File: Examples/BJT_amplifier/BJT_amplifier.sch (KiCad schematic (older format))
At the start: 12 parts, among them Q1 NPN

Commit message: Modified Example
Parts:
- R1, R2, R3, R4, R5, R6: symbol R -> R-RESCUE-BJT_amplifier
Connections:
- net labels added: out
- wire segments 24 -> 26
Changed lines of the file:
@@
 EESchema Schematic File Version 2
+LIBS:BJT_amplifier-rescue
+LIBS:eSim_Analog
+LIBS:eSim_Devices
+LIBS:eSim_Digital
+LIBS:eSim_Hybrid
+LIBS:eSim_Miscellaneous
+LIBS:eSim_Sources
+LIBS:eSim_Subckt
+LIBS:eSim_User
 LIBS:power
 LIBS:device
@@
 LIBS:memory
 LIBS:xilinx
-LIBS:special
 LIBS:microcontrollers
 LIBS:dsp
@@
 LIBS:contrib
 LIBS:valves
-LIBS:eSim_Analog
-LIBS:eSim_Devices
-LIBS:eSim_Digital
-LIBS:eSim_Hybrid
-LIBS:eSim_Sources
 LIBS:BJT_amplifier-cache
 EELAYER 25 0
@@
 $EndComp
 $Comp
-L GND #PWR02
+L GND-RESCUE-BJT_amplifier #PWR02
 U 1 1 51A47FCD
 P 5650 4850
@@
 $EndComp
 $Comp
-L R R1
+L R-RESCUE-BJT_amplifier R1
 U 1 1 51A47FBC
 P 4050 3600
@@
 $EndComp
 $Comp
-L R R2
+L R-RESCUE-BJT_amplifier R2
 U 1 1 51A47FAB
 P 5100 3050
@@
 $EndComp
 $Comp
-L R R3
+L R-RESCUE-BJT_amplifier R3
 U 1 1 51A47F97
 P 5100 4200
@@
 $EndComp
 $Comp
-L R R6
+L R-RESCUE-BJT_amplifier R6
 U 1 1 51A47F8B
 P 7050 4200
@@
 $EndComp
 $Comp
-L R R5
+L R-RESCUE-BJT_amplifier R5
 U 1 1 51A47F5C
 P 6100 3050
@@
 $EndComp
 $Comp
-L R R4
+L R-RESCUE-BJT_amplifier R4
 U 1 1 51A47F50
 P 5850 4200
@@
 Wire Wire Line
 	5100 2900 5100 2800
+Text GLabel 7000 3250 2    60   Input ~ 0
+out
+Wire Wire Line
+	7000 3250 6950 3250
+Wire Wire Line
+	6950 3250 6950 3300
+Connection ~ 6950 3300
 $EndSCHEMATC

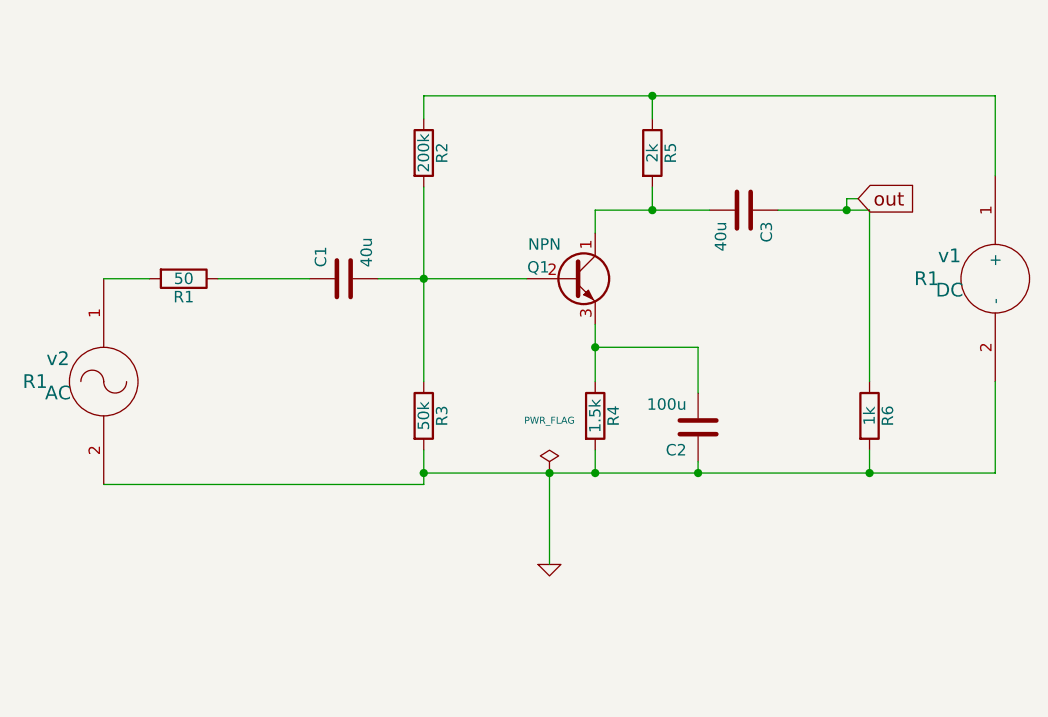
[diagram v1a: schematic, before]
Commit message: Remove unwanted example
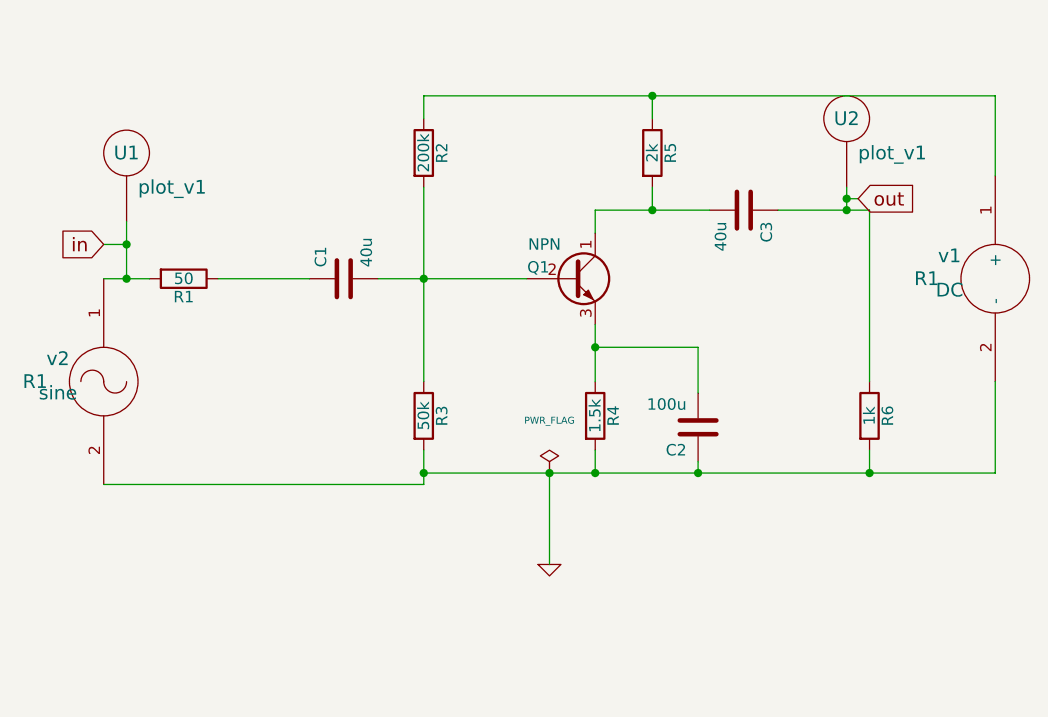
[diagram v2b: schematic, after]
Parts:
- removed v2: AC, R1, symbol AC
- added U1, U2: plot_v1, symbol plot_v1
- added v2: sine, R1, symbol sine
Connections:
- net GND: now also v2.2 (-)
- net out: now also U2.~
- net in: now reaches R1.2
- net in: now also U1.~, v2.1 (+)
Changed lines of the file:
@@
 LIBS:eSim_Hybrid
 LIBS:eSim_Miscellaneous
+LIBS:eSim_Plot
+LIBS:eSim_Power
 LIBS:eSim_Sources
 LIBS:eSim_Subckt
@@
 $EndComp
 $Comp
-L AC v2
-U 1 1 51A486A5
-P 3700 4050
-F 0 "v2" H 3500 4150 60  0000 C CNN
-F 1 "AC" H 3500 4000 60  0000 C CNN
-F 2 "R1" H 3400 4050 60  0000 C CNN
-F 3 "" H 3700 4050 60  0001 C CNN
-	1    3700 4050
-	1    0    0    -1
-$EndComp
-$Comp
 L PWR_FLAG #FLG01
 U 1 1 51A48298
@@
 	7000 3250 6950 3250
 Wire Wire Line
-	6950 3250 6950 3300
+	6950 3200 6950 3300
 Connection ~ 6950 3300
+Text GLabel 3700 3450 0    60   Input ~ 0
+in
+Wire Wire Line
+	3700 3450 3800 3450
+Wire Wire Line
+	3800 3350 3800 3600
+Connection ~ 3800 3600
+$Comp
+L plot_v1 U1
+U 1 1 56D444F7
+P 3800 3550
+F 0 "U1" H 3800 4050 60  0000 C CNN
+F 1 "plot_v1" H 4000 3900 60  0000 C CNN
+F 2 "" H 3800 3550 60  0000 C CNN
+F 3 "" H 3800 3550 60  0000 C CNN
+	1    3800 3550
+	1    0    0    -1
+$EndComp
+$Comp
+L plot_v1 U2
+U 1 1 56D4460A
+P 6950 3400
+F 0 "U2" H 6950 3900 60  0000 C CNN
+F 1 "plot_v1" H 7150 3750 60  0000 C CNN
+F 2 "" H 6950 3400 60  0000 C CNN
+F 3 "" H 6950 3400 60  0000 C CNN
+	1    6950 3400
+	1    0    0    -1
+$EndComp
+Connection ~ 6950 3250
+Connection ~ 3800 3450
+$Comp
+L sine v2
+U 1 1 56D44890
+P 3700 4050
+F 0 "v2" H 3500 4150 60  0000 C CNN
+F 1 "sine" H 3500 4000 60  0000 C CNN
+F 2 "R1" H 3400 4050 60  0000 C CNN
+F 3 "" H 3700 4050 60  0000 C CNN
+	1    3700 4050
+	1    0    0    -1
+$EndComp
 $EndSCHEMATC

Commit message: common code for Win and Linux, merged py2 changes
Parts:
- removed Q1: NPN, symbol NPN
- added Q1: eSim_NPN, symbol eSim_NPN
- v1: symbol DC -> DC-RESCUE-BJT_amplifier
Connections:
- net at C2.2, R4.1: now also Q1.3 (E)
- net at C3.2, R5.2: now also Q1.1 (C)
- net at C1.2, R2.2, R3.1: now also Q1.2 (B)
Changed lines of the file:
@@
 Connection ~ 6100 2800
 $Comp
-L DC v1
+L DC-RESCUE-BJT_amplifier v1
 U 1 1 51A5D97E
 P 7600 3600
@@
 	1    0    0    -1
 $EndComp
-$Comp
-L NPN Q1
-U 1 1 557583B4
-P 5750 3600
-F 0 "Q1" H 5650 3650 50  0000 R CNN
-F 1 "NPN" H 5700 3750 50  0000 R CNN
-F 2 "" H 5950 3700 29  0000 C CNN
-F 3 "" H 5750 3600 60  0000 C CNN
-	1    5750 3600
-	1    0    0    -1
-$EndComp
 Wire Wire Line
 	6100 2900 6100 2800
@@
 	1    0    0    -1
 $EndComp
+$Comp
+L eSim_NPN Q1
+U 1 1 5D5CED6B
+P 5750 3600
+F 0 "Q1" H 5650 3650 50  0000 R CNN
+F 1 "eSim_NPN" H 5700 3750 50  0000 R CNN
+F 2 "" H 5950 3700 29  0000 C CNN
+F 3 "" H 5750 3600 60  0000 C CNN
+	1    5750 3600
+	1    0    0    -1
+$EndComp
